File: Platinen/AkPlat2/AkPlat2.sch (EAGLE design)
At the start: 12 parts, among them CON1 XT30UPB-M, X1 332-02, X2 332-02, X3 332-02, X4 332-02

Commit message: platine verbessert
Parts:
- removed X1, X2, X3, X4: 332-02, con-garry:332-02
- added SV1, SV2: (no value), con-lstb:MA04-1
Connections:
- net N$16: now also SV1.1; no longer X1-2.S
- net N$17: now also SV1.2; no longer X1-1.S
- net N$18: now also SV1.3; no longer X2-2.S
- net N$19: now also SV1.4; no longer X2-1.S
- net N$20: now also SV2.1; no longer X3-2.S
- net N$21: now also SV2.2; no longer X3-1.S
- net N$22: now also SV2.3; no longer X4-2.S
- net N$23: now also SV2.4; no longer X4-1.S
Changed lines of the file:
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@@
 <part name="ARDUINO_NANO1" library="ArduinoNanoV30" deviceset="ARDUINO_NANO" device=""/>
 <part name="CON1" library="amass" deviceset="XT30" device="UPB-M"/>
-<part name="X1" library="con-garry" library_urn="urn:adsk.eagle:library:147" deviceset="332-02" device="" package3d_urn="urn:adsk.eagle:package:6810/1"/>
-<part name="X2" library="con-garry" library_urn="urn:adsk.eagle:library:147" deviceset="332-02" device="" package3d_urn="urn:adsk.eagle:package:6810/1"/>
-<part name="X3" library="con-garry" library_urn="urn:adsk.eagle:library:147" deviceset="332-02" device="" package3d_urn="urn:adsk.eagle:package:6810/1"/>
-<part name="X4" library="con-garry" library_urn="urn:adsk.eagle:library:147" deviceset="332-02" device="" package3d_urn="urn:adsk.eagle:package:6810/1"/>
 <part name="U$1" library="Motorcontroller" deviceset="CONTROLLER" device=""/>
 <part name="U$2" library="Motorcontroller" deviceset="CONTROLLER" device=""/>
@@
 <part name="JP3" library="pinhead" library_urn="urn:adsk.eagle:library:325" deviceset="PINHD-1X3" device="" package3d_urn="urn:adsk.eagle:package:22458/2"/>
 <part name="JP4" library="pinhead" library_urn="urn:adsk.eagle:library:325" deviceset="PINHD-1X3" device="" package3d_urn="urn:adsk.eagle:package:22458/2"/>
+<part name="SV1" library="con-lstb" library_urn="urn:adsk.eagle:library:162" deviceset="MA04-1" device="" package3d_urn="urn:adsk.eagle:package:8337/1"/>
+<part name="SV2" library="con-lstb" library_urn="urn:adsk.eagle:library:162" deviceset="MA04-1" device="" package3d_urn="urn:adsk.eagle:package:8337/1"/>
 </parts>
 <sheets>
@@
 <attribute name="NAME" x="175.768" y="49.53" size="1.778" layer="95" rot="R90"/>
 </instance>
-<instance part="X1" gate="-1" x="185.42" y="101.6" smashed="yes" rot="R90">
-<attribute name="NAME" x="186.182" y="104.14" size="1.524" layer="95" rot="R90"/>
-<attribute name="VALUE" x="184.023" y="100.838" size="1.778" layer="96" rot="R90"/>
-</instance>
-<instance part="X1" gate="-2" x="185.42" y="121.92" smashed="yes" rot="R90">
-<attribute name="NAME" x="186.182" y="124.46" size="1.524" layer="95" rot="R90"/>
-<attribute name="VALUE" x="184.023" y="121.158" size="1.778" layer="96" rot="R90"/>
-</instance>
-<instance part="X2" gate="-1" x="185.42" y="66.04" smashed="yes" rot="R90">
-<attribute name="NAME" x="186.182" y="68.58" size="1.524" layer="95" rot="R90"/>
-<attribute name="VALUE" x="184.023" y="65.278" size="1.778" layer="96" rot="R90"/>
-</instance>
-<instance part="X2" gate="-2" x="185.42" y="86.36" smashed="yes" rot="R90">
-<attribute name="NAME" x="186.182" y="88.9" size="1.524" layer="95" rot="R90"/>
-<attribute name="VALUE" x="184.023" y="85.598" size="1.778" layer="96" rot="R90"/>
-</instance>
-<instance part="X3" gate="-1" x="185.42" y="15.24" smashed="yes" rot="R90">
-<attribute name="NAME" x="186.182" y="17.78" size="1.524" layer="95" rot="R90"/>
-<attribute name="VALUE" x="184.023" y="14.478" size="1.778" layer="96" rot="R90"/>
-</instance>
-<instance part="X3" gate="-2" x="185.42" y="35.56" smashed="yes" rot="R90">
-<attribute name="NAME" x="186.182" y="38.1" size="1.524" layer="95" rot="R90"/>
-<attribute name="VALUE" x="184.023" y="34.798" size="1.778" layer="96" rot="R90"/>
-</instance>
-<instance part="X4" gate="-1" x="185.42" y="-20.32" smashed="yes" rot="R90">
-<attribute name="NAME" x="186.182" y="-17.78" size="1.524" layer="95" rot="R90"/>
-<attribute name="VALUE" x="184.023" y="-21.082" size="1.778" layer="96" rot="R90"/>
-</instance>
-<instance part="X4" gate="-2" x="185.42" y="0" smashed="yes" rot="R90">
-<attribute name="NAME" x="186.182" y="2.54" size="1.524" layer="95" rot="R90"/>
-<attribute name="VALUE" x="184.023" y="-0.762" size="1.778" layer="96" rot="R90"/>
-</instance>
 <instance part="U$1" gate="G$1" x="149.86" y="76.2" smashed="yes" rot="R180"/>
 <instance part="U$2" gate="G$1" x="149.86" y="45.72" smashed="yes" rot="R180"/>
@@
 <attribute name="NAME" x="27.305" y="29.21" size="1.778" layer="95" rot="R90"/>
 <attribute name="VALUE" x="40.64" y="29.21" size="1.778" layer="96" rot="R90"/>
+</instance>
+<instance part="SV1" gate="1" x="198.12" y="93.98" smashed="yes" rot="R180">
+<attribute name="VALUE" x="199.39" y="104.14" size="1.778" layer="96" rot="R180"/>
+<attribute name="NAME" x="199.39" y="88.138" size="1.778" layer="95" rot="R180"/>
+</instance>
+<instance part="SV2" gate="1" x="198.12" y="2.54" smashed="yes" rot="R180">
+<attribute name="VALUE" x="199.39" y="12.7" size="1.778" layer="96" rot="R180"/>
+<attribute name="NAME" x="199.39" y="-3.302" size="1.778" layer="95" rot="R180"/>
 </instance>
 </instances>
@@
 <wire x1="149.86" y1="73.66" x2="154.94" y2="73.66" width="0.1524" layer="91"/>
 <wire x1="154.94" y1="73.66" x2="154.94" y2="119.38" width="0.1524" layer="91"/>
-<pinref part="X1" gate="-2" pin="S"/>
-<wire x1="154.94" y1="119.38" x2="185.42" y2="119.38" width="0.1524" layer="91"/>
+<wire x1="154.94" y1="119.38" x2="182.88" y2="121.92" width="0.1524" layer="91"/>
+<pinref part="SV1" gate="1" pin="1"/>
+<wire x1="182.88" y1="121.92" x2="190.5" y2="121.92" width="0.1524" layer="91"/>
+<wire x1="190.5" y1="121.92" x2="190.5" y2="99.06" width="0.1524" layer="91"/>
 </segment>
 </net>
 <net name="N$17" class="0">
 <segment>
-<pinref part="X1" gate="-1" pin="S"/>
 <wire x1="185.42" y1="99.06" x2="157.48" y2="99.06" width="0.1524" layer="91"/>
 <wire x1="157.48" y1="99.06" x2="157.48" y2="71.12" width="0.1524" layer="91"/>
 <pinref part="U$1" gate="G$1" pin="3"/>
 <wire x1="157.48" y1="71.12" x2="149.86" y2="71.12" width="0.1524" layer="91"/>
+<wire x1="185.42" y1="99.06" x2="185.42" y2="96.52" width="0.1524" layer="91"/>
+<pinref part="SV1" gate="1" pin="2"/>
+<wire x1="185.42" y1="96.52" x2="190.5" y2="96.52" width="0.1524" layer="91"/>
 </segment>
 </net>
@@
 <wire x1="149.86" y1="68.58" x2="160.02" y2="68.58" width="0.1524" layer="91"/>
 <wire x1="160.02" y1="68.58" x2="160.02" y2="83.82" width="0.1524" layer="91"/>
-<pinref part="X2" gate="-2" pin="S"/>
 <wire x1="160.02" y1="83.82" x2="185.42" y2="83.82" width="0.1524" layer="91"/>
+<pinref part="SV1" gate="1" pin="3"/>
+<wire x1="190.5" y1="93.98" x2="185.42" y2="93.98" width="0.1524" layer="91"/>
+<wire x1="185.42" y1="93.98" x2="185.42" y2="83.82" width="0.1524" layer="91"/>
 </segment>
 </net>
 <net name="N$19" class="0">
 <segment>
-<pinref part="X2" gate="-1" pin="S"/>
-<wire x1="185.42" y1="63.5" x2="160.02" y2="63.5" width="0.1524" layer="91"/>
+<wire x1="187.96" y1="63.5" x2="160.02" y2="63.5" width="0.1524" layer="91"/>
 <wire x1="160.02" y1="63.5" x2="160.02" y2="66.04" width="0.1524" layer="91"/>
 <pinref part="U$1" gate="G$1" pin="5"/>
 <wire x1="160.02" y1="66.04" x2="149.86" y2="66.04" width="0.1524" layer="91"/>
+<pinref part="SV1" gate="1" pin="4"/>
+<wire x1="187.96" y1="63.5" x2="187.96" y2="91.44" width="0.1524" layer="91"/>
+<wire x1="187.96" y1="91.44" x2="190.5" y2="91.44" width="0.1524" layer="91"/>
 </segment>
 </net>
@@
 <wire x1="149.86" y1="43.18" x2="177.8" y2="43.18" width="0.1524" layer="91"/>
 <wire x1="177.8" y1="43.18" x2="177.8" y2="33.02" width="0.1524" layer="91"/>
-<pinref part="X3" gate="-2" pin="S"/>
-<wire x1="177.8" y1="33.02" x2="185.42" y2="33.02" width="0.1524" layer="91"/>
+<wire x1="177.8" y1="33.02" x2="190.5" y2="33.02" width="0.1524" layer="91"/>
+<pinref part="SV2" gate="1" pin="1"/>
+<wire x1="190.5" y1="33.02" x2="190.5" y2="7.62" width="0.1524" layer="91"/>
 </segment>
 </net>
@@
 <wire x1="149.86" y1="40.64" x2="175.26" y2="40.64" width="0.1524" layer="91"/>
 <wire x1="175.26" y1="40.64" x2="175.26" y2="12.7" width="0.1524" layer="91"/>
-<pinref part="X3" gate="-1" pin="S"/>
-<wire x1="175.26" y1="12.7" x2="185.42" y2="12.7" width="0.1524" layer="91"/>
+<wire x1="175.26" y1="12.7" x2="187.96" y2="12.7" width="0.1524" layer="91"/>
+<wire x1="187.96" y1="12.7" x2="187.96" y2="5.08" width="0.1524" layer="91"/>
+<pinref part="SV2" gate="1" pin="2"/>
+<wire x1="187.96" y1="5.08" x2="190.5" y2="5.08" width="0.1524" layer="91"/>
 </segment>
 </net>
@@
 <wire x1="149.86" y1="38.1" x2="172.72" y2="38.1" width="0.1524" layer="91"/>
 <wire x1="172.72" y1="38.1" x2="172.72" y2="-2.54" width="0.1524" layer="91"/>
-<pinref part="X4" gate="-2" pin="S"/>
 <wire x1="172.72" y1="-2.54" x2="185.42" y2="-2.54" width="0.1524" layer="91"/>
+<wire x1="185.42" y1="-2.54" x2="185.42" y2="2.54" width="0.1524" layer="91"/>
+<pinref part="SV2" gate="1" pin="3"/>
+<wire x1="185.42" y1="2.54" x2="190.5" y2="2.54" width="0.1524" layer="91"/>
 </segment>
 </net>
@@
 <pinref part="U$2" gate="G$1" pin="5"/>
 <wire x1="149.86" y1="35.56" x2="170.18" y2="35.56" width="0.1524" layer="91"/>
-<pinref part="X4" gate="-1" pin="S"/>
 <wire x1="170.18" y1="35.56" x2="170.18" y2="-22.86" width="0.1524" layer="91"/>
-<wire x1="170.18" y1="-22.86" x2="185.42" y2="-22.86" width="0.1524" layer="91"/>
-</segment>
-</net>
+<wire x1="170.18" y1="-22.86" x2="190.5" y2="-22.86" width="0.1524" layer="91"/>
+<pinref part="SV2" gate="1" pin="4"/>
+<wire x1="190.5" y1="-22.86" x2="190.5" y2="0" width="0.1524" layer="91"/>
+</segment>
+</net>

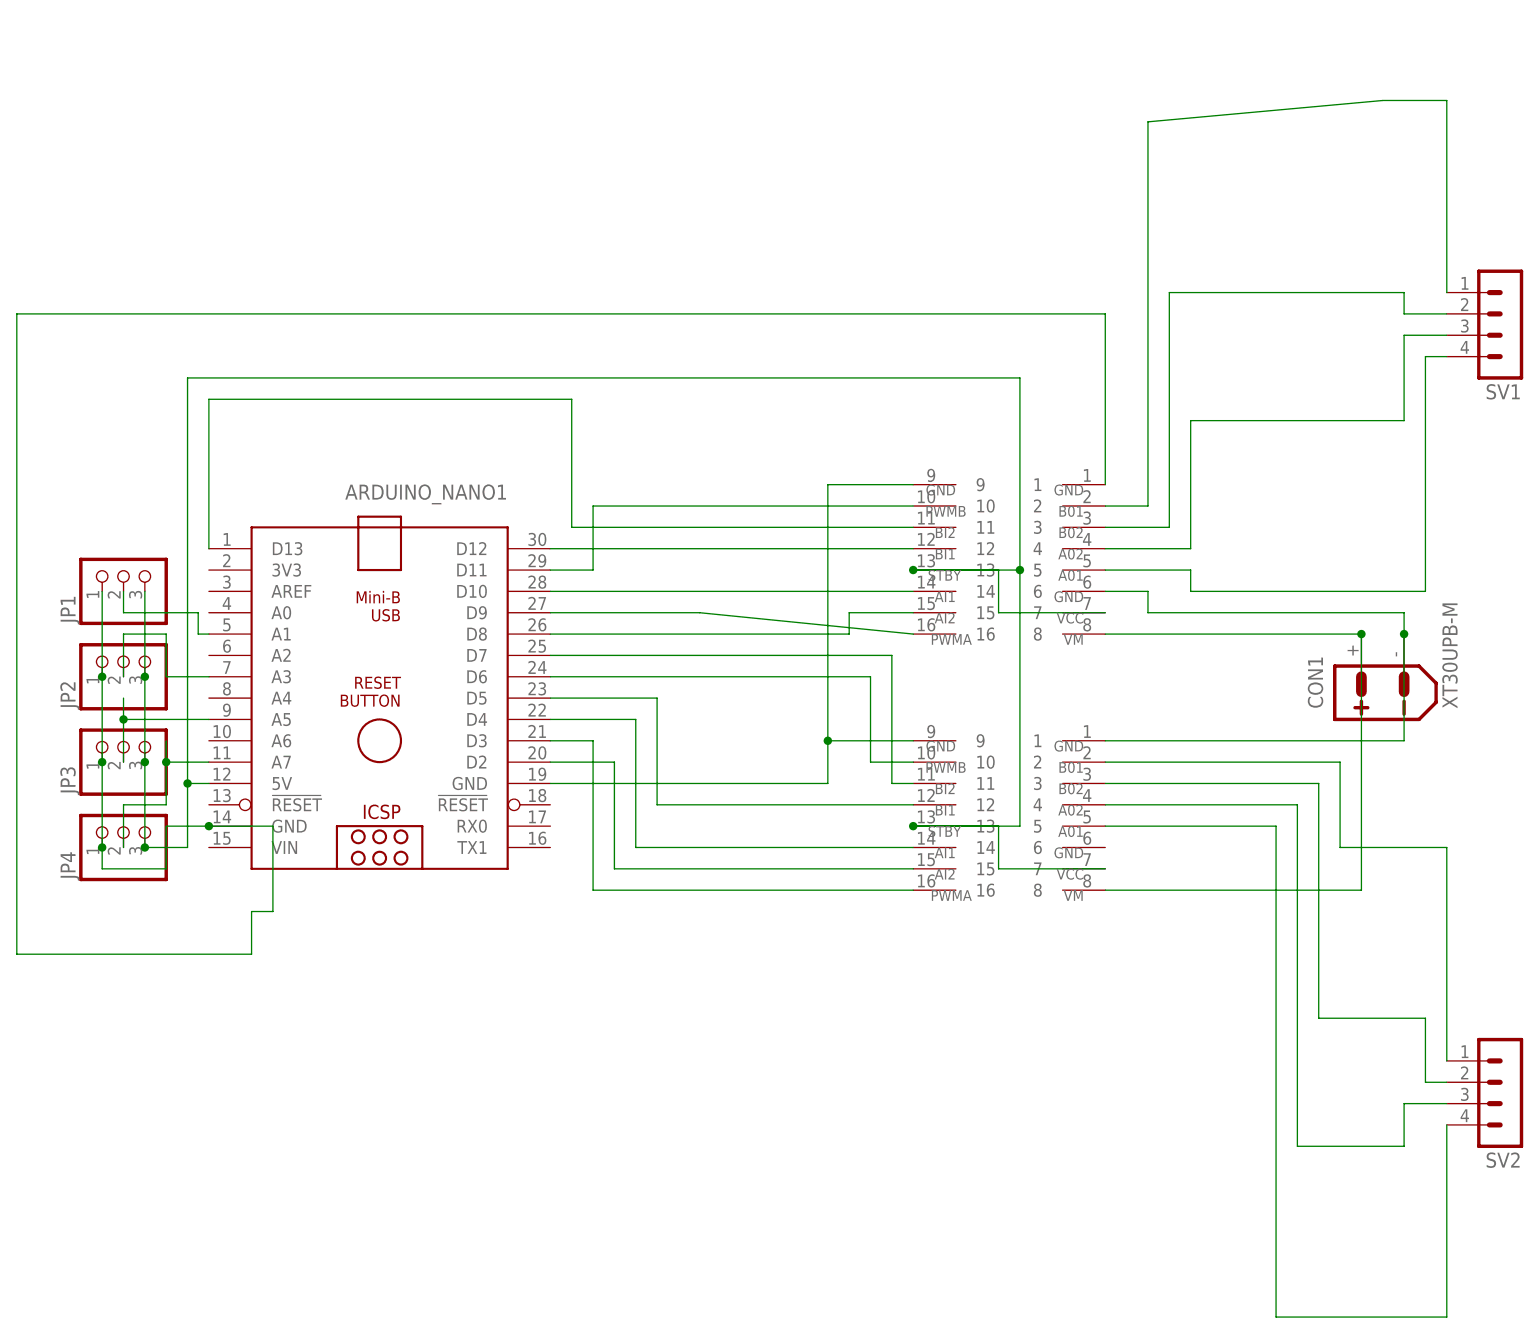
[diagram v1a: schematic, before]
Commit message: Platine changes and smother movement
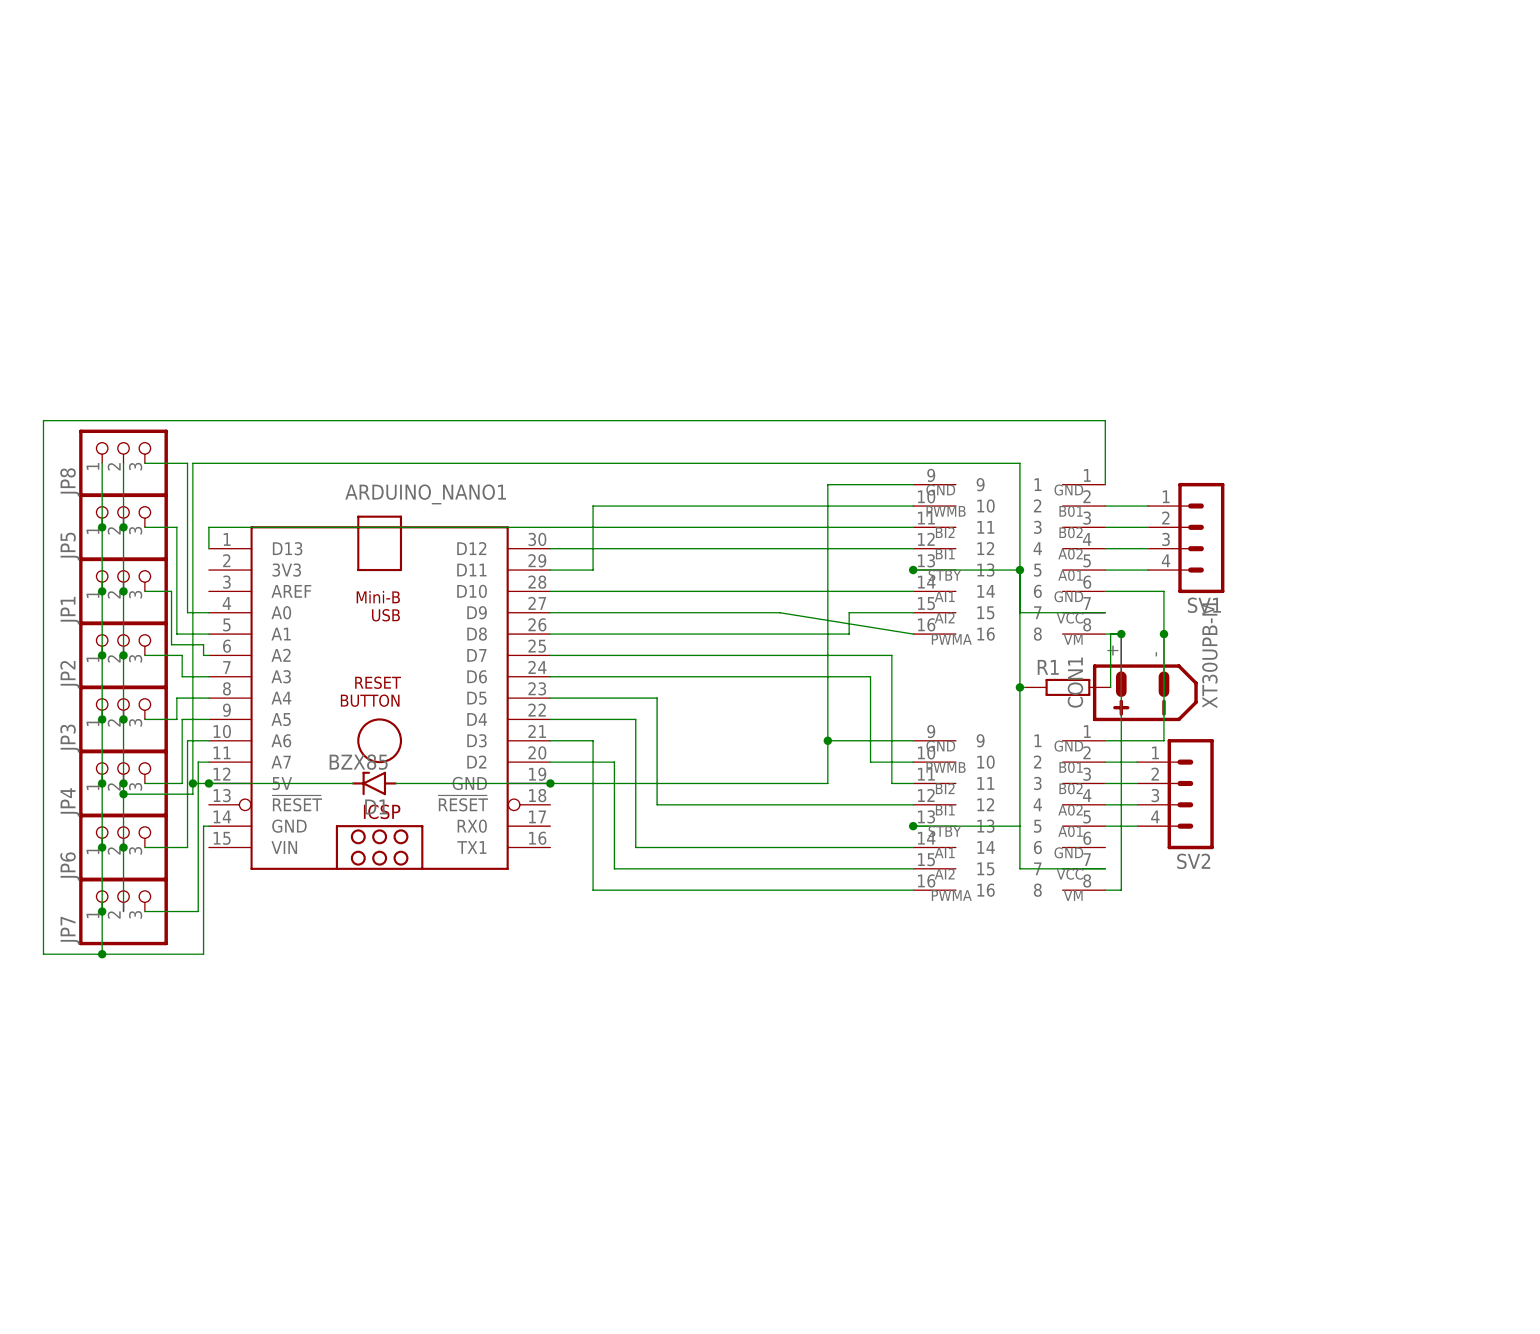
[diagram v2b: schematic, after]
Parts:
- added D1: BZX85, diode:BZX85
- added JP5, JP6, JP7, JP8: (no value), pinhead:PINHD-1X3
- added R1: (no value), rcl:R-EU_0204/7
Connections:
- removed net N$24: ARDUINO_NANO1.GND@2, JP1.1, JP2.1, JP3.1, JP4.1, U$1.1
- removed net N$25: ARDUINO_NANO1.A1, JP1.2
- new net N$30: ARDUINO_NANO1.A5, JP4.3
- new net N$31: ARDUINO_NANO1.A4, JP3.3
- new net N$32: ARDUINO_NANO1.A3, JP2.3
- new net N$33: ARDUINO_NANO1.A2, JP1.3
- new net N$34: ARDUINO_NANO1.A1, JP5.3
- new net N$35: ARDUINO_NANO1.A0, JP8.3
- net N$1: now also D1.A
- net N$15: now also ARDUINO_NANO1.GND@2, JP1.1, JP2.1, JP3.1, JP4.1, JP5.1, JP6.1, JP7.1, JP8.1, U$1.1; no longer ARDUINO_NANO1.A3, JP2.2
- net N$26: now also ARDUINO_NANO1.A7, JP7.3; no longer ARDUINO_NANO1.A5, JP3.2
- net N$27: now also ARDUINO_NANO1.A6, JP6.3; no longer ARDUINO_NANO1.A7, JP4.2
- net N$28: now also D1.C, JP1.2, JP2.2, JP3.2, JP4.2, JP5.2, JP6.2, JP7.2, JP8.2, R1.1; no longer JP1.3, JP2.3, JP3.3, JP4.3
- net N$8: now also R1.2
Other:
- moved on the sheet: CON1, JP2, JP3, JP4, SV1, SV2

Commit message: PCB almost done
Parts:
- removed SV1, SV2: (no value), con-lstb:MA04-1
- added JP10, JP11, JP12, JP9: (no value), pinhead:PINHD-1X2
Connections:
- net N$28 renamed 5V
- net N$8 renamed VM
- removed net N$1: ARDUINO_NANO1.GND@1, D1.A, U$1.9, U$2.9
- removed net N$15: ARDUINO_NANO1.GND@2, JP1.1, JP2.1, JP3.1, JP4.1, JP5.1, JP6.1, JP7.1, JP8.1, U$1.1
- removed net N$2: CON1.-, U$1.6, U$2.1
- new net GND: ARDUINO_NANO1.GND@1, ARDUINO_NANO1.GND@2, CON1.-, D1.A, JP1.1, JP2.1, JP3.1, JP4.1, JP5.1, JP6.1, JP7.1, JP8.1, U$1.1, U$1.6, U$1.9, U$2.1, U$2.6, U$2.9
- net N$16: now also JP9.1; no longer SV1.1
- net N$17: now also JP9.2; no longer SV1.2
- net N$18: now also JP10.1; no longer SV1.3
- net N$19: now also JP10.2; no longer SV1.4
- net N$20: now also JP11.1; no longer SV2.1
- net N$21: now also JP11.2; no longer SV2.2
- net N$22: now also JP12.1; no longer SV2.3
- net N$23: now also JP12.2; no longer SV2.4

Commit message: PCB fertig Gerber fertig
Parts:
- removed CON1: XT30UPB-M, amass:XT30UPB-M
- removed JP1, JP2, JP3, JP4, JP5, JP6, JP7, JP8: (no value), pinhead:PINHD-1X3
- removed JP10, JP11, JP12, JP9: (no value), pinhead:PINHD-1X2
- removed R1: (no value), rcl:R-EU_0204/7
- added 1.1, 1.2, 2.1, 2.2, 3.1, 3.2, 4.1, 4.2: 22-23-2031, con-molex:22-23-2031
- added 100Ω: 100, rcl:R-EU_0204/7
- added M1, M2, M3, M4: 22-23-2021, con-molex:22-23-2021
- added POWER: XT30UPB-M, amass:XT30UPB-M
- renumbered ARDUINO_NANO1 to ARDUINO_NANO, D1 to ZENER_5V1
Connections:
- net 5V: now also 1.1-2.S, 1.2-2.S, 100Ω.1, 2.1-2.S, 2.2-2.S, 3.1-2.S, 3.2-2.S, 4.1-2.S, 4.2-2.S; no longer JP1.2, JP2.2, JP3.2, JP4.2, JP5.2, JP6.2, JP7.2, JP8.2, R1.1
- net GND: now also 1.1-1.S, 1.2-1.S, 2.1-1.S, 2.2-1.S, 3.1-1.S, 3.2-1.S, 4.1-1.S, 4.2-1.S, POWER.-; no longer CON1.-, JP1.1, JP2.1, JP3.1, JP4.1, JP5.1, JP6.1, JP7.1, JP8.1
- net N$16: now also M1-1.S; no longer JP9.1
- net N$17: now also M1-2.S; no longer JP9.2
- net N$18: now also M2-1.S; no longer JP10.1
- net N$19: now also M2-2.S; no longer JP10.2
- net N$20: now also M3-1.S; no longer JP11.1
- net N$21: now also M3-2.S; no longer JP11.2
- net N$22: now also M4-1.S; no longer JP12.1
- net N$23: now also M4-2.S; no longer JP12.2
- net N$26: now also 4.2-3.S; no longer JP7.3
- net N$27: now also 4.1-3.S; no longer JP6.3
- net N$30: now also 3.1-3.S; no longer JP4.3
- net N$31: now also 3.2-3.S; no longer JP3.3
- net N$32: now also 2.1-3.S; no longer JP2.3
- net N$33: now also 2.2-3.S; no longer JP1.3
- net N$34: now also 1.1-3.S; no longer JP5.3
- net N$35: now also 1.2-3.S; no longer JP8.3
- net VM: now also 100Ω.2, POWER.+; no longer CON1.+, R1.2
